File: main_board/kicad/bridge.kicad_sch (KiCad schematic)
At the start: 21 parts, among them Q1 IRFB3077, Q2 IRFB3077, Q3 IRFB3077, Q4 IRFB3077, Q5 IRFB3077, Q6 IRFB3077

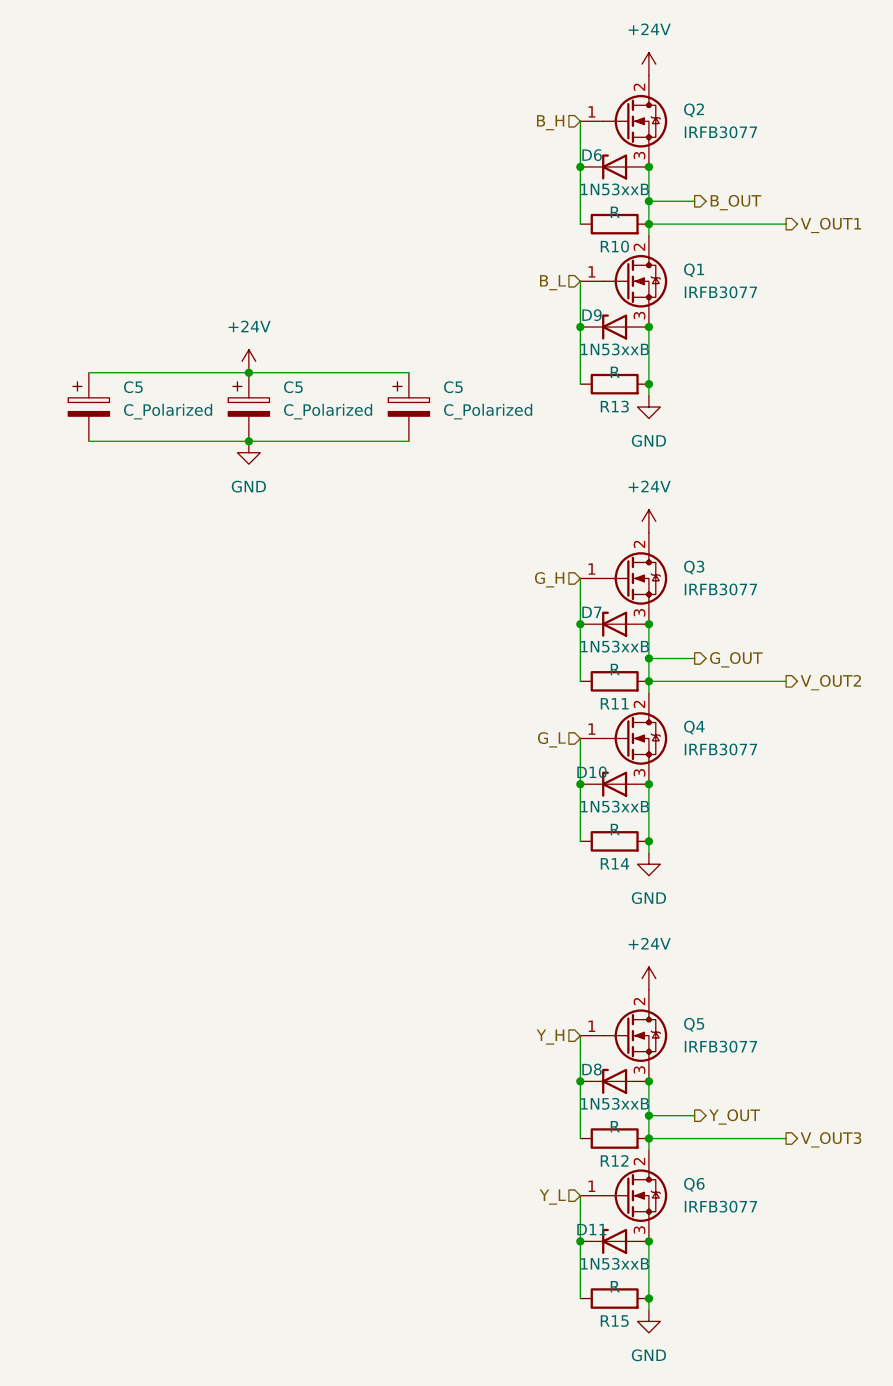
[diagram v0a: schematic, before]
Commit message: added ISP socket for attiny
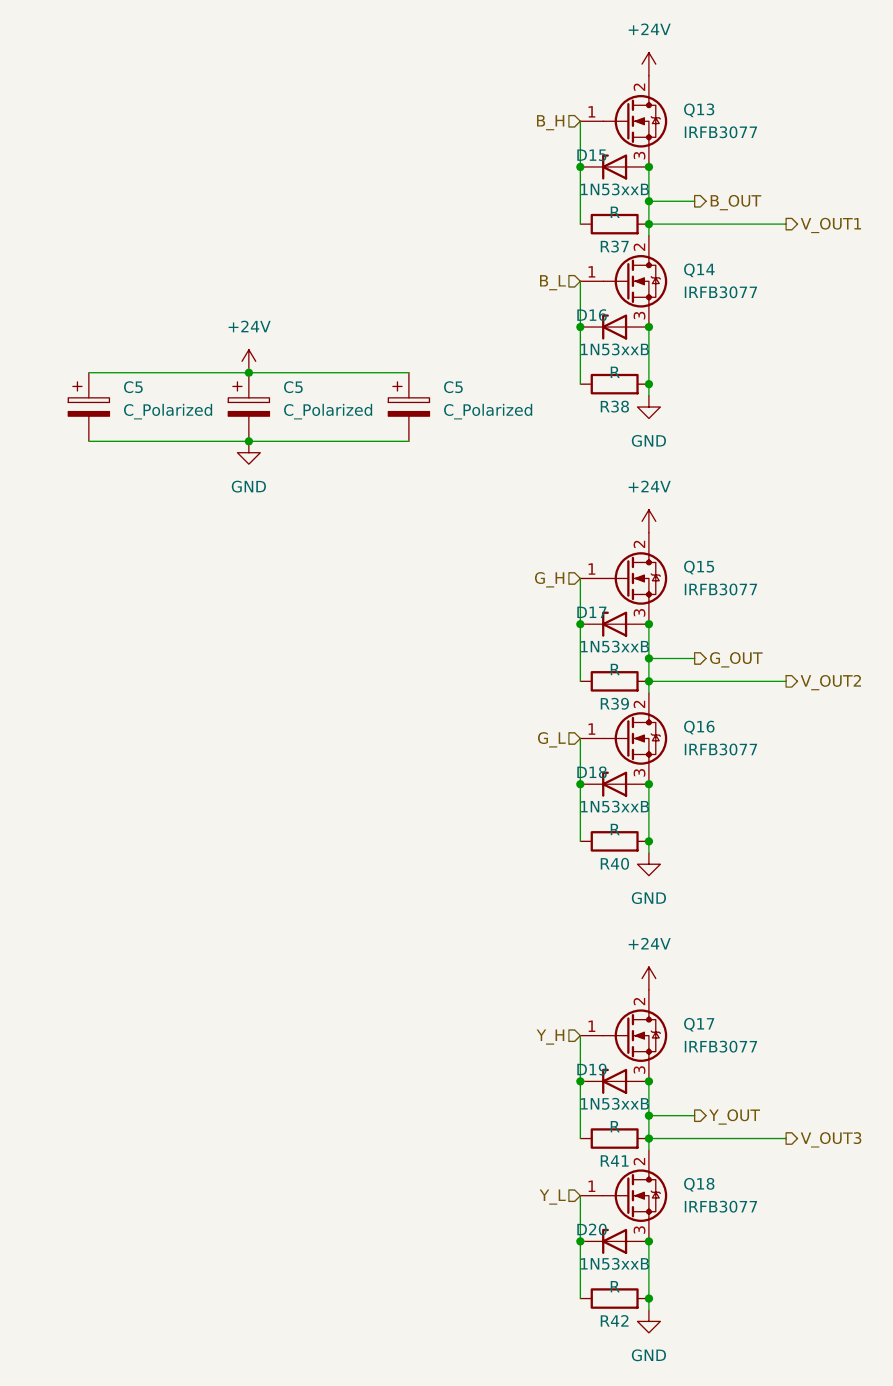
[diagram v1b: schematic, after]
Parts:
- renumbered D6 to D15, D9 to D16, D7 to D17, D10 to D18, D8 to D19, D11 to D20, Q2 to Q13, Q1 to Q14, Q3 to Q15, Q4 to Q16, Q5 to Q17, Q6 to Q18, R10 to R37, R13 to R38, R11 to R39, R14 to R40, R12 to R41, R15 to R42
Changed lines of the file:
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@@
   (symbol (lib_id "Device:R") (at 113.03 166.37 90) (unit 1)
     (in_bom yes) (on_board yes) (dnp no)
-    (property "Reference" "R15" (at 113.03 168.91 90)
+    (property "Reference" "R42" (at 113.03 168.91 90)
       (effects (font (size 1.27 1.27)))
     )
@@
           (reference "R13") (unit 1)
         )
-        (path "/9139d8e7-a5dc-421f-9a12-f77d83384a16/fbdcc8f5-3f4a-4b6d-8bd9-dcde8bb62812"
-          (reference "R15") (unit 1)
-        )
       )
     )
@@
   (symbol (lib_id "2022-lsd:IRFB3077") (at 114.3 137.16 0) (unit 1)
     (in_bom yes) (on_board yes) (dnp no) (fields_autoplaced)
-    (property "Reference" "Q5" (at 120.65 135.89 0)
+    (property "Reference" "Q17" (at 120.65 135.89 0)
       (effects (font (size 1.27 1.27)) (justify left))
     )
@@
   (symbol (lib_id "Device:R") (at 113.03 64.77 90) (unit 1)
     (in_bom yes) (on_board yes) (dnp no)
-    (property "Reference" "R13" (at 113.03 67.31 90)
+    (property "Reference" "R38" (at 113.03 67.31 90)
       (effects (font (size 1.27 1.27)))
     )
@@
   (symbol (lib_id "Device:R") (at 113.03 148.59 90) (unit 1)
     (in_bom yes) (on_board yes) (dnp no)
-    (property "Reference" "R12" (at 113.03 151.13 90)
+    (property "Reference" "R41" (at 113.03 151.13 90)
       (effects (font (size 1.27 1.27)))
     )
@@
   (symbol (lib_id "2022-lsd:IRFB3077") (at 114.3 86.36 0) (unit 1)
     (in_bom yes) (on_board yes) (dnp no)
-    (property "Reference" "Q3" (at 120.65 85.09 0)
+    (property "Reference" "Q15" (at 120.65 85.09 0)
       (effects (font (size 1.27 1.27)) (justify left))
     )
@@
   (symbol (lib_id "power:+24V") (at 116.84 81.28 0) (unit 1)
     (in_bom yes) (on_board yes) (dnp no) (fields_autoplaced)
-    (property "Reference" "#PWR013" (at 116.84 85.09 0)
+    (property "Reference" "#PWR069" (at 116.84 85.09 0)
       (effects (font (size 1.27 1.27)) hide)
     )
@@
   (symbol (lib_id "power:+24V") (at 72.39 63.5 0) (unit 1)
     (in_bom yes) (on_board yes) (dnp no) (fields_autoplaced)
-    (property "Reference" "#PWR012" (at 72.39 67.31 0)
+    (property "Reference" "#PWR065" (at 72.39 67.31 0)
       (effects (font (size 1.27 1.27)) hide)
     )
@@
   (symbol (lib_id "Diode:1N53xxB") (at 113.03 160.02 0) (unit 1)
     (in_bom yes) (on_board yes) (dnp no)
-    (property "Reference" "D11" (at 110.49 158.75 0)
+    (property "Reference" "D20" (at 110.49 158.75 0)
       (effects (font (size 1.27 1.27)))
     )
@@
           (reference "D8") (unit 1)
         )
-        (path "/9139d8e7-a5dc-421f-9a12-f77d83384a16/fbdcc8f5-3f4a-4b6d-8bd9-dcde8bb62812"
-          (reference "D11") (unit 1)
-        )
       )
     )
@@
   (symbol (lib_id "Diode:1N53xxB") (at 113.03 109.22 0) (unit 1)
     (in_bom yes) (on_board yes) (dnp no)
-    (property "Reference" "D10" (at 110.49 107.95 0)
+    (property "Reference" "D18" (at 110.49 107.95 0)
       (effects (font (size 1.27 1.27)))
     )
@@
           (reference "D6") (unit 1)
         )
-        (path "/9139d8e7-a5dc-421f-9a12-f77d83384a16/fbdcc8f5-3f4a-4b6d-8bd9-dcde8bb62812"
-          (reference "D10") (unit 1)
-        )
       )
     )
@@
   (symbol (lib_id "2022-lsd:IRFB3077") (at 114.3 154.94 0) (unit 1)
     (in_bom yes) (on_board yes) (dnp no) (fields_autoplaced)
-    (property "Reference" "Q6" (at 120.65 153.67 0)
+    (property "Reference" "Q18" (at 120.65 153.67 0)
       (effects (font (size 1.27 1.27)) (justify left))
     )
@@
   (symbol (lib_id "Diode:1N53xxB") (at 113.03 142.24 0) (unit 1)
     (in_bom yes) (on_board yes) (dnp no)
-    (property "Reference" "D8" (at 110.49 140.97 0)
+    (property "Reference" "D19" (at 110.49 140.97 0)
       (effects (font (size 1.27 1.27)))
     )
@@
           (reference "D7") (unit 1)
         )
-        (path "/9139d8e7-a5dc-421f-9a12-f77d83384a16/fbdcc8f5-3f4a-4b6d-8bd9-dcde8bb62812"
-          (reference "D8") (unit 1)
-        )
       )
     )
@@
   (symbol (lib_id "Device:R") (at 113.03 97.79 90) (unit 1)
     (in_bom yes) (on_board yes) (dnp no)
-    (property "Reference" "R11" (at 113.03 100.33 90)
+    (property "Reference" "R39" (at 113.03 100.33 90)
       (effects (font (size 1.27 1.27)))
     )
@@
           (reference "R10") (unit 1)
         )
-        (path "/9139d8e7-a5dc-421f-9a12-f77d83384a16/fbdcc8f5-3f4a-4b6d-8bd9-dcde8bb62812"
-          (reference "R11") (unit 1)
-        )
       )
     )
@@
   (symbol (lib_id "power:GND") (at 116.84 66.04 0) (unit 1)
     (in_bom yes) (on_board yes) (dnp no) (fields_autoplaced)
-    (property "Reference" "#PWR010" (at 116.84 72.39 0)
+    (property "Reference" "#PWR068" (at 116.84 72.39 0)
       (effects (font (size 1.27 1.27)) hide)
     )
@@
   (symbol (lib_id "power:+24V") (at 116.84 30.48 0) (unit 1)
     (in_bom yes) (on_board yes) (dnp no) (fields_autoplaced)
-    (property "Reference" "#PWR09" (at 116.84 34.29 0)
+    (property "Reference" "#PWR067" (at 116.84 34.29 0)
       (effects (font (size 1.27 1.27)) hide)
     )
@@
   (symbol (lib_id "Device:R") (at 113.03 46.99 90) (unit 1)
     (in_bom yes) (on_board yes) (dnp no)
-    (property "Reference" "R10" (at 113.03 49.53 90)
+    (property "Reference" "R37" (at 113.03 49.53 90)
       (effects (font (size 1.27 1.27)))
     )
@@
           (reference "R8") (unit 1)
         )
-        (path "/9139d8e7-a5dc-421f-9a12-f77d83384a16/fbdcc8f5-3f4a-4b6d-8bd9-dcde8bb62812"
-          (reference "R10") (unit 1)
-        )
       )
     )
@@
   (symbol (lib_id "power:GND") (at 72.39 71.12 0) (unit 1)
     (in_bom yes) (on_board yes) (dnp no) (fields_autoplaced)
-    (property "Reference" "#PWR011" (at 72.39 77.47 0)
+    (property "Reference" "#PWR066" (at 72.39 77.47 0)
       (effects (font (size 1.27 1.27)) hide)
     )
@@
   (symbol (lib_id "2022-lsd:IRFB3077") (at 114.3 53.34 0) (unit 1)
     (in_bom yes) (on_board yes) (dnp no) (fields_autoplaced)
-    (property "Reference" "Q1" (at 120.65 52.07 0)
+    (property "Reference" "Q14" (at 120.65 52.07 0)
       (effects (font (size 1.27 1.27)) (justify left))
     )
@@
   (symbol (lib_id "Diode:1N53xxB") (at 113.03 40.64 0) (unit 1)
     (in_bom yes) (on_board yes) (dnp no)
-    (property "Reference" "D6" (at 110.49 39.37 0)
+    (property "Reference" "D15" (at 110.49 39.37 0)
       (effects (font (size 1.27 1.27)))
     )
@@
           (reference "D2") (unit 1)
         )
-        (path "/9139d8e7-a5dc-421f-9a12-f77d83384a16/fbdcc8f5-3f4a-4b6d-8bd9-dcde8bb62812"
-          (reference "D6") (unit 1)
-        )
       )
     )
@@
   (symbol (lib_id "power:GND") (at 116.84 116.84 0) (unit 1)
     (in_bom yes) (on_board yes) (dnp no) (fields_autoplaced)
-    (property "Reference" "#PWR014" (at 116.84 123.19 0)
+    (property "Reference" "#PWR070" (at 116.84 123.19 0)
       (effects (font (size 1.27 1.27)) hide)
     )
@@
           (reference "#PWR027") (unit 1)
         )
-        (path "/9139d8e7-a5dc-421f-9a12-f77d83384a16/fbdcc8f5-3f4a-4b6d-8bd9-dcde8bb62812"
-          (reference "#PWR014") (unit 1)
-        )
       )
     )
@@
   (symbol (lib_id "power:+24V") (at 116.84 132.08 0) (unit 1)
     (in_bom yes) (on_board yes) (dnp no) (fields_autoplaced)
-    (property "Reference" "#PWR015" (at 116.84 135.89 0)
+    (property "Reference" "#PWR071" (at 116.84 135.89 0)
       (effects (font (size 1.27 1.27)) hide)
     )
@@
   (symbol (lib_id "power:GND") (at 116.84 167.64 0) (unit 1)
     (in_bom yes) (on_board yes) (dnp no) (fields_autoplaced)
-    (property "Reference" "#PWR016" (at 116.84 173.99 0)
+    (property "Reference" "#PWR072" (at 116.84 173.99 0)
       (effects (font (size 1.27 1.27)) hide)
     )
@@
           (reference "#PWR029") (unit 1)
         )
-        (path "/9139d8e7-a5dc-421f-9a12-f77d83384a16/fbdcc8f5-3f4a-4b6d-8bd9-dcde8bb62812"
-          (reference "#PWR016") (unit 1)
-        )
       )
     )
@@
   (symbol (lib_id "Device:R") (at 113.03 115.57 90) (unit 1)
     (in_bom yes) (on_board yes) (dnp no)
-    (property "Reference" "R14" (at 113.03 118.11 90)
+    (property "Reference" "R40" (at 113.03 118.11 90)
       (effects (font (size 1.27 1.27)))
     )
@@
           (reference "R11") (unit 1)
         )
-        (path "/9139d8e7-a5dc-421f-9a12-f77d83384a16/fbdcc8f5-3f4a-4b6d-8bd9-dcde8bb62812"
-          (reference "R14") (unit 1)
-        )
       )
     )
@@
   (symbol (lib_id "2022-lsd:IRFB3077") (at 114.3 104.14 0) (unit 1)
     (in_bom yes) (on_board yes) (dnp no)
-    (property "Reference" "Q4" (at 120.65 102.87 0)
+    (property "Reference" "Q16" (at 120.65 102.87 0)
       (effects (font (size 1.27 1.27)) (justify left))
     )
@@
   (symbol (lib_id "Diode:1N53xxB") (at 113.03 91.44 0) (unit 1)
     (in_bom yes) (on_board yes) (dnp no)
-    (property "Reference" "D7" (at 110.49 90.17 0)
+    (property "Reference" "D17" (at 110.49 90.17 0)
       (effects (font (size 1.27 1.27)))
     )
@@
         (path "/9139d8e7-a5dc-421f-9a12-f77d83384a16/b730c020-dbf9-4624-b380-91471479f30c/4903fc77-158c-4e4e-9ffc-8865d087d3f3"
           (reference "D4") (unit 1)
-        )
-        (path "/9139d8e7-a5dc-421f-9a12-f77d83384a16/fbdcc8f5-3f4a-4b6d-8bd9-dcde8bb62812"
-          (reference "D7") (unit 1)
         )
       )
@@
   (symbol (lib_id "2022-lsd:IRFB3077") (at 114.3 35.56 0) (unit 1)
     (in_bom yes) (on_board yes) (dnp no) (fields_autoplaced)
-    (property "Reference" "Q2" (at 120.65 34.29 0)
+    (property "Reference" "Q13" (at 120.65 34.29 0)
       (effects (font (size 1.27 1.27)) (justify left))
     )
@@
   (symbol (lib_id "Diode:1N53xxB") (at 113.03 58.42 0) (unit 1)
     (in_bom yes) (on_board yes) (dnp no)
-    (property "Reference" "D9" (at 110.49 57.15 0)
+    (property "Reference" "D16" (at 110.49 57.15 0)
       (effects (font (size 1.27 1.27)))
     )
@@
           (reference "D3") (unit 1)
         )
-        (path "/9139d8e7-a5dc-421f-9a12-f77d83384a16/fbdcc8f5-3f4a-4b6d-8bd9-dcde8bb62812"
-          (reference "D9") (unit 1)
-        )
-      )
+      )

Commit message: added component values to bridge
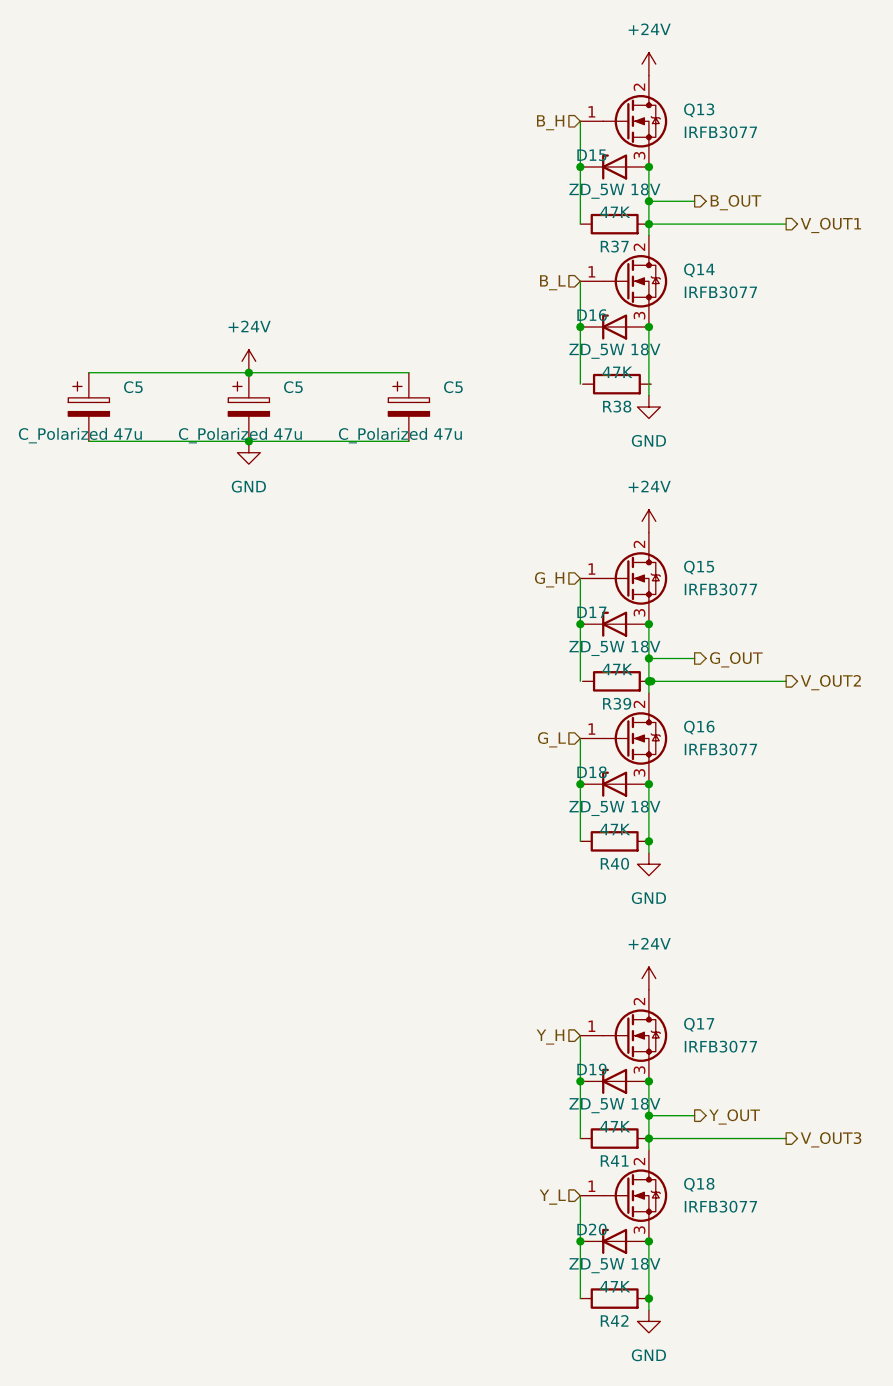
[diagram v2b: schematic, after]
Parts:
- C5: value C_Polarized -> C_Polarized 47u
- D15, D16, D17, D18, D19, D20: value 1N53xxB -> ZD_5W 18V
- R37, R38, R39, R40, R41, R42: value R -> 47K
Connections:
- net B_L: no longer R38.1
- net GND: no longer R38.2
- net G_H: no longer R39.1

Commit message: renamed motor magic file
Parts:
- renumbered D15 to D2, D16 to D3, D17 to D4, D18 to D6, D19 to D7, D20 to D8, Q13 to Q1, Q14 to Q2, Q15 to Q3, Q16 to Q4, Q17 to Q5, Q18 to Q6, R39 to R10, R40 to R11, R41 to R12, R42 to R13, R37 to R8, R38 to R9
